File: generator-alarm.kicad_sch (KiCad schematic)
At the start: 25 parts, among them J1 Sensor, J2 UART, J3 SWD, J4 12V, SW1 RESET, U1 RA-02, U2 STM32F030K6Tx, U3 XC6206P332PR-G

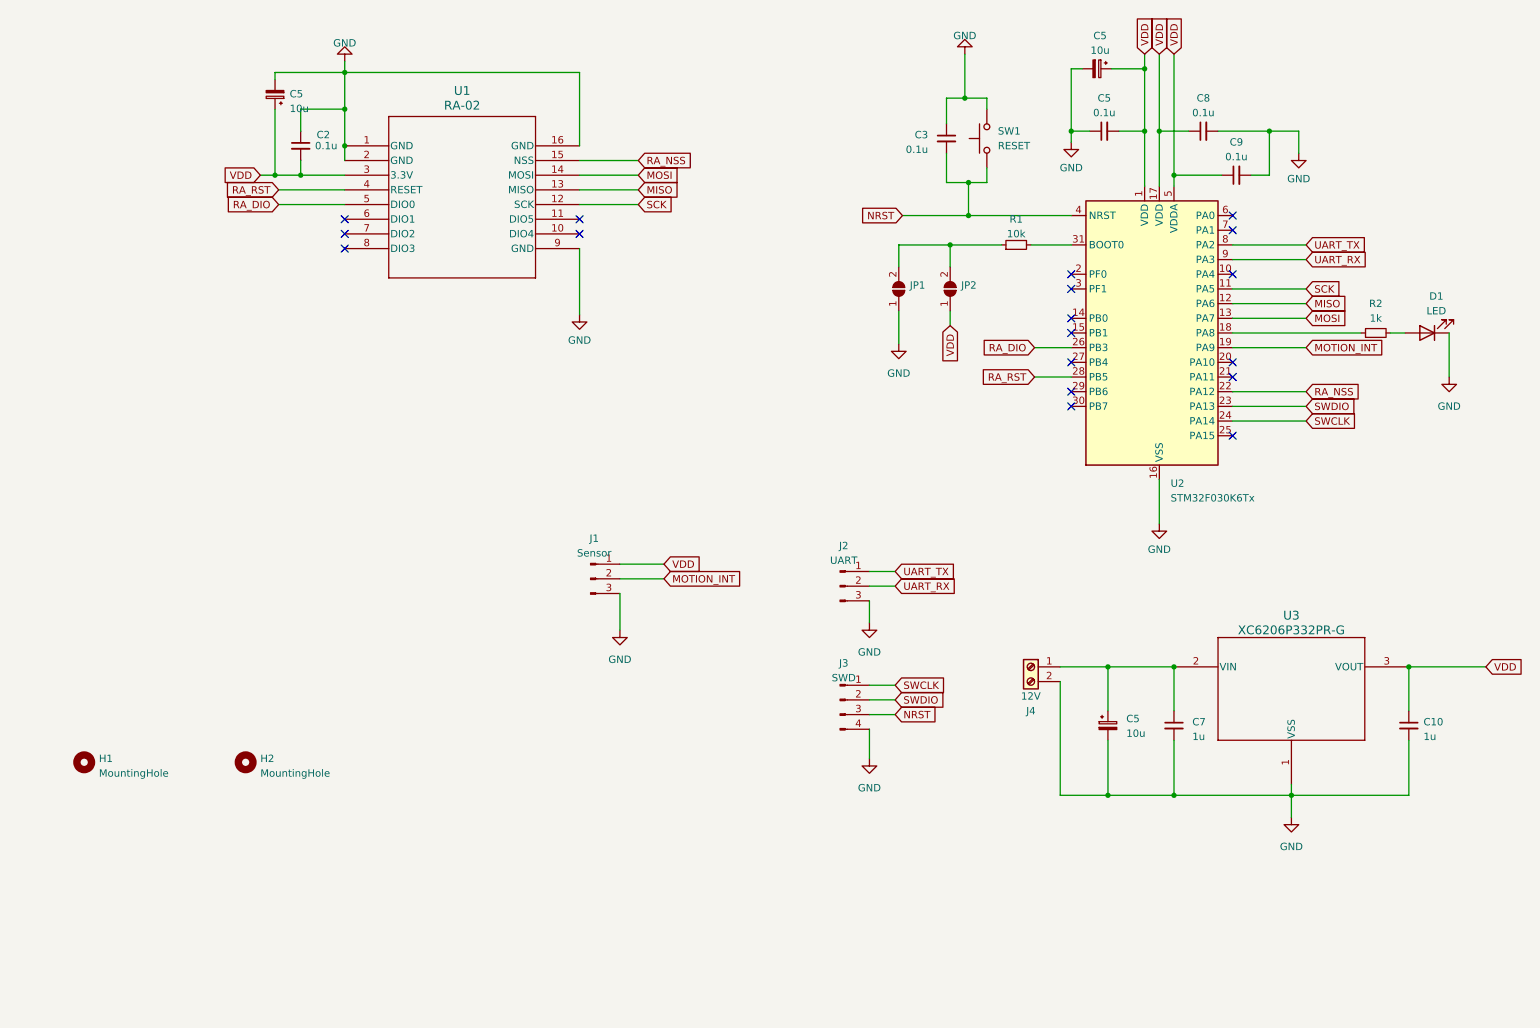
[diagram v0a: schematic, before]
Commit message: Add USB-C connector and Li-Ion charger controller
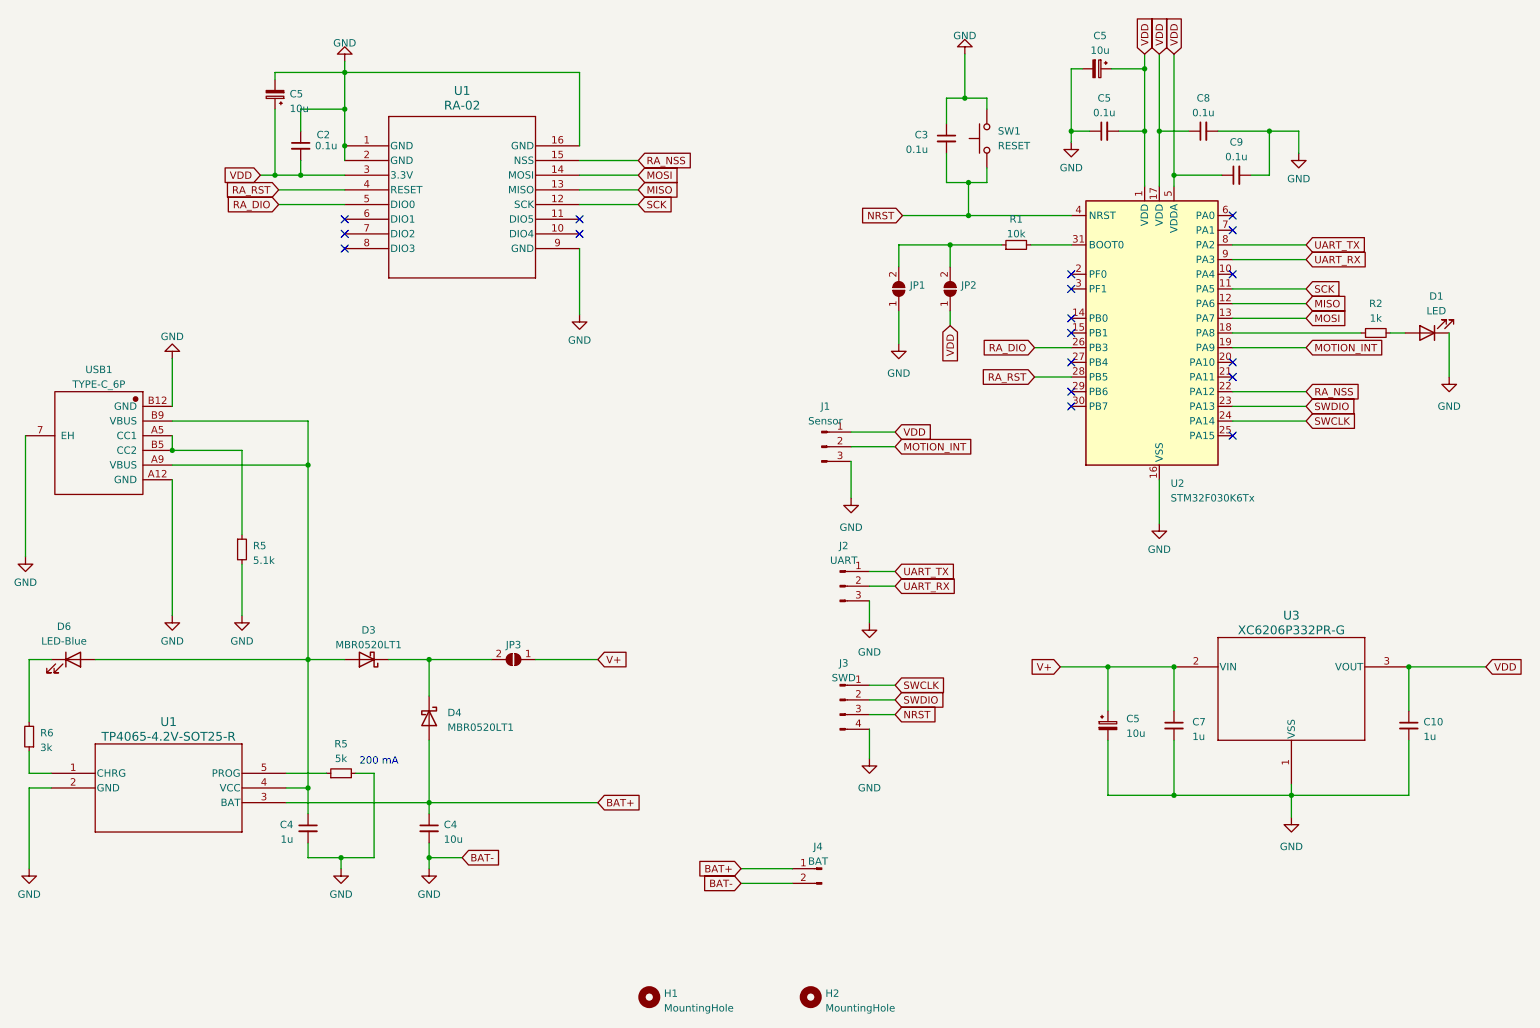
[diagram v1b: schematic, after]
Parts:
- removed J4: 12V, TerminalBlock_4Ucon:TerminalBlock_4Ucon_1x02_P3.50mm_Vertical, symbol Connector:Screw_Terminal_01x02
- added C4: 10u, Capacitor_SMD:C_0603_1608Metric, symbol Device:C_Small
- added C4: 1u, Capacitor_SMD:C_0603_1608Metric, symbol Device:C_Small
- added D3, D4: MBR0520LT1, Diode_SMD:D_SOD-123, symbol Device:D_Schottky
- added D6: LED-Blue, LED_SMD:LED_0805_2012Metric, symbol Device:LED
- added J4: BAT, Connector_PinHeader_1.27mm:PinHeader_1x02_P1.27mm_Vertical, symbol Connector:Conn_01x02_Pin
- added JP3: SolderJumper_2_Open, Jumper:SolderJumper-2_P1.3mm_Open_RoundedPad1.0x1.5mm, symbol Jumper:SolderJumper_2_Open
- added R5: 5.1k, Resistor_SMD:R_0805_2012Metric, symbol Device:R_Small
- added R5: 5k, Resistor_SMD:R_0603_1608Metric, symbol Device:R_Small
- added R6: 3k, Resistor_SMD:R_0603_1608Metric, symbol Device:R_Small
- added U1: TP4065-4.2V-SOT25-R, footprints2:SOT-23-5L_TPW, symbol 2023-08-21_19-03-02:TP4065-4.2V-SOT25-R
- added USB1: TYPE-C_6P, kicad_lceda:TYPE-C-SMD_TYPE-C-6P, symbol kicad_lceda:TYPE-C_6P
- D1: footprint LED_SMD:LED_1206_3216Metric -> LED_SMD:LED_0805_2012Metric
- J2: footprint Connector_PinHeader_2.54mm:PinHeader_1x03_P2.54mm_Vertical -> Connector_PinHeader_1.27mm:PinHeader_1x03_P1.27mm_Vertical
- J3: footprint Connector_PinHeader_2.54mm:PinHeader_1x04_P2.54mm_Vertical -> Connector_PinHeader_1.27mm:PinHeader_1x04_P1.27mm_Vertical
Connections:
- net GND: now also C4.2, C4.2, J4.2 (Pin_2), R5.2, R5.2, U1.2 (GND), USB1.7 (EH), USB1.A12 (GND), USB1.B12 (GND)
- net V+: now reaches C5.1, C7.1, U3.2 (VIN)
- net V+: now also JP3.1 (A)
- new net: R6.1, U1.1 (CHRG)
- new net: D6.1 (K), R6.2
- new net: D3.1 (K), D4.1 (K), JP3.2 (B)
- new net: C4.1, D3.2 (A), D6.2 (A), U1.4 (VCC), USB1.A9 (VBUS), USB1.B9 (VBUS)
- new net: R5.1, USB1.A5 (CC1), USB1.B5 (CC2)
- new net: R5.1, U1.5 (PROG)
- new net BAT+: C4.1, D4.2 (A), J4.1 (Pin_1), U1.3 (BAT)
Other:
- note added: "200 mA"
- moved on the sheet: H1, H2, J1
